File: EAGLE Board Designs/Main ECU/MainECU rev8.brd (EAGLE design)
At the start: 120.6 x 78.9 mm, 218 parts, among them J1 JUMPER, J2 JUMPER, J3 JUMPER, J4 JUMPER, J5 JUMPER, J6 JUMPER, J7 JUMPER, J8 JUMPER, P1 SOLDER_PAD, P2 SOLDER_PAD, Q1 P-CHANNEL_MOSFET_DMP3099L-7, Q12 P-CHANNEL_MOSFET_DMP3099L-7, X1 CONNECTOR-37, X2 CONNECTOR-4AUTOSPORT, X3 CONNECTOR-4NANO-FIT-VERTICAL-4, X4 CONNECTOR-4NANO-FIT-VERTICAL-4

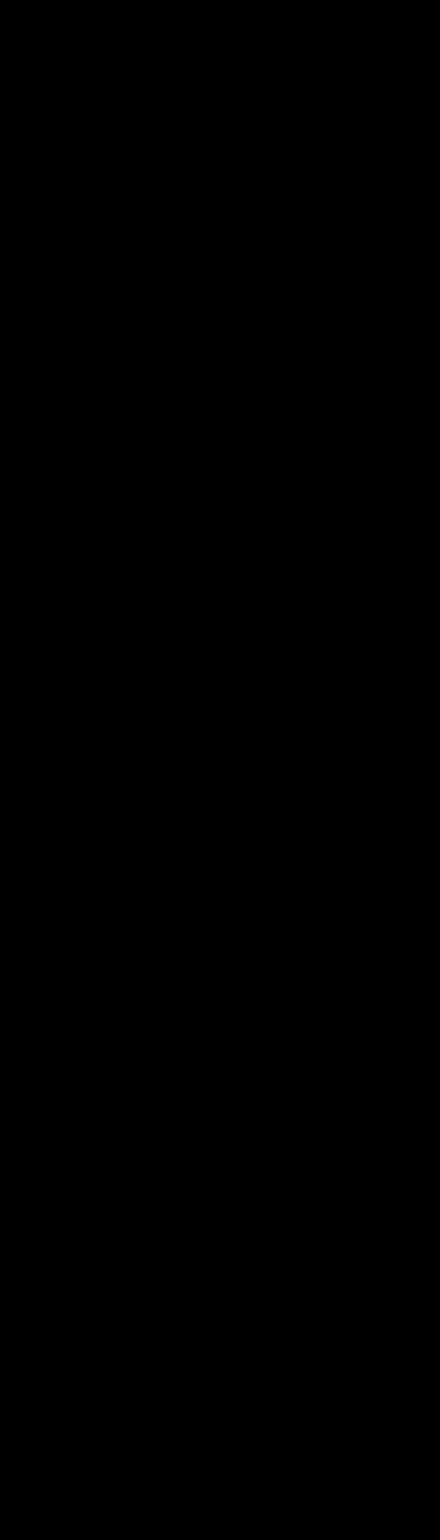
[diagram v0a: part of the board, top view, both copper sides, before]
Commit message: added BSPD schematic
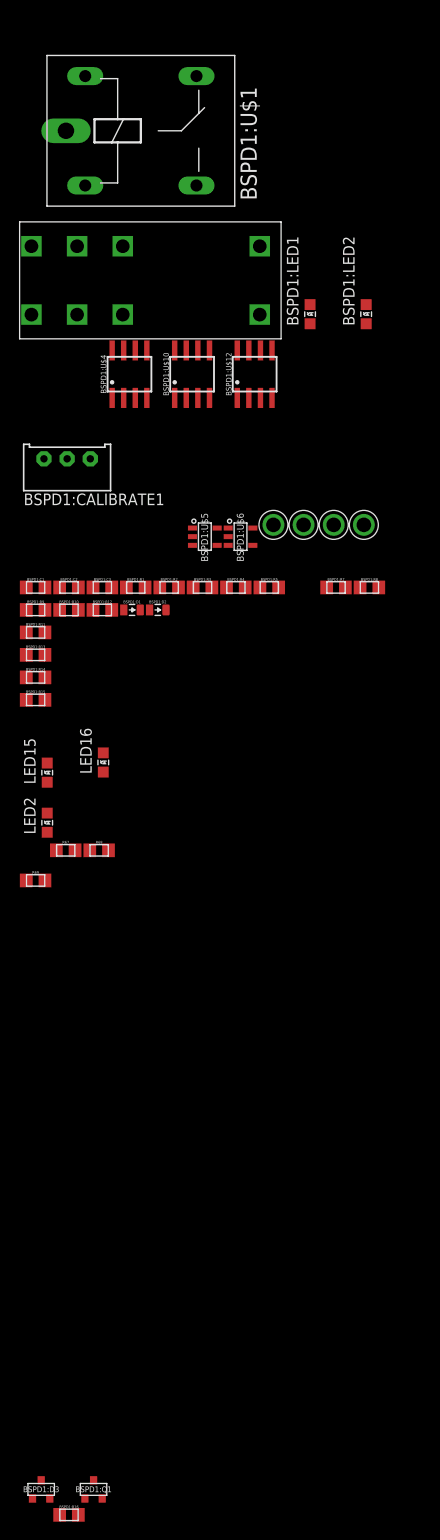
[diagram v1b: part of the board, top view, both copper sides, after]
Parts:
- added BSPD1:C1: .47µ, HyTechDevices:0805
- added BSPD1:C2, BSPD1:C3: 2.2µ, HyTechDevices:0805
- added BSPD1:CALIBRATE1: (no value), HyTechDevices:TRIMPOT_3296
- added BSPD1:D1, BSPD1:D2: DIODE0805, HyTechDevices:0805_D
- added BSPD1:D3: MMBZ5246BLT1G, HyTechDevices:SOT23
- added BSPD1:LED1, LED2: RED, HyTechDevices:LED-805
- added BSPD1:LED2, LED15: YELLOW, HyTechDevices:LED-805
- added BSPD1:Q1: (no value), HyTechDevices:SOT23
- added BSPD1:R1: 12k, HyTechDevices:0805
- added BSPD1:R10, BSPD1:R12: 100, HyTechDevices:0805
- added BSPD1:R11, BSPD1:R13, BSPD1:R14, BSPD1:R15: TBD, HyTechDevices:0805
- added BSPD1:R16, BSPD1:R4, BSPD1:R7: 10k, HyTechDevices:0805
- added BSPD1:R2: 43k, HyTechDevices:0805
- added BSPD1:R3: 330, HyTechDevices:0805
- added BSPD1:R5: 680k, HyTechDevices:0805
- added BSPD1:R8, BSPD1:R9, R67, R68: 270, HyTechDevices:0805
- added BSPD1:U$1: G5LE, HyTechDevices:ZF112
- added BSPD1:U$10, BSPD1:U$4: MCP6542SOIC, HyTechDevices:SOIC-08
- added BSPD1:U$11, BSPD1:U$13, U$14, U$15: TEST_POINT, HyTechDevices:TEST_POINT
- added BSPD1:U$12: MCP6002SOIC, HyTechDevices:SOIC-08
- added BSPD1:U$3: JW2SN-DC12V, HyTechDevices:JW2SN
- added BSPD1:U$5: SN74AHC1G09, HyTechDevices:SOT-23-5
- added BSPD1:U$6: SN74LVC1G08, HyTechDevices:SOT-23-5
- added LED16: GREEN, HyTechDevices:LED-805
- added R69: 200, HyTechDevices:0805
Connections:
- new net BSPD1:N$1: BSPD1:D1.A, BSPD1:Q1.3, BSPD1:U$3.COIL+
- new net BSPD1:N$10: BSPD1:D1.C
- new net BSPD1:N$13: BSPD1:C1.1, BSPD1:R3.1, BSPD1:R5.1, BSPD1:U$12.3, BSPD1:U$4.3
- new net BSPD1:N$14: BSPD1:LED2.C, BSPD1:R8.1
- new net BSPD1:N$15: BSPD1:LED1.C, BSPD1:R9.1
- new net BSPD1:N$16: BSPD1:LED1.A, BSPD1:U$10.7, BSPD1:U$11.P$1, BSPD1:U$5.2, BSPD1:U$6.2
- new net BSPD1:N$17: BSPD1:LED2.A, BSPD1:U$10.1, BSPD1:U$13.P$1, BSPD1:U$5.1, BSPD1:U$6.1
- new net BSPD1:N$2: BSPD1:R3.2, BSPD1:U$5.4
- new net BSPD1:N$3: BSPD1:D3.3, BSPD1:Q1.1, BSPD1:R16.1, BSPD1:U$4.1
- new net BSPD1:N$5: BSPD1:R14.2, BSPD1:R15.1, BSPD1:U$10.2
- new net BSPD1:N$6: BSPD1:CALIBRATE1.2, BSPD1:U$10.6
- new net BSPD1:N$7: BSPD1:R11.2, BSPD1:R13.1, BSPD1:U$4.2
- new net BSPD1:N$9: BSPD1:R1.2, BSPD1:R2.1, BSPD1:U$12.5
- new net BSPD1:SHUTDOWN_C: BSPD1:U$1.S, BSPD1:U$3.6
- new net BSPD1:SIGNAL_BRAKE_FILT: BSPD1:C3.2, BSPD1:R12.2, BSPD1:R4.2, BSPD1:U$10.5
- new net BSPD1:SIGNAL_CURRENT_FILT: BSPD1:C2.2, BSPD1:R10.2, BSPD1:R7.1, BSPD1:U$10.3
- new net N$64: LED2.C, R67.2
- new net N$76: LED15.C, R68.2
- new net N$77: LED16.C, R69.2
- new net READ_CHARGE: BSPD1:U$12.1, BSPD1:U$12.2, LED15.A
- new net READ_FAULT: BSPD1:U$12.6, BSPD1:U$12.7, LED16.A
- new net READ_SWITCH: BSPD1:U$6.4, LED2.A
- new net SIGNAL_CURRENT: BSPD1:R10.1, U$15.P$1
- net +12V: now also BSPD1:D2.C, BSPD1:R2.2, BSPD1:U$1.2, BSPD1:U$3.3, BSPD1:U$3.4, BSPD1:U$3.COIL-
- net +5V: now also BSPD1:CALIBRATE1.1, BSPD1:R13.2, BSPD1:R15.2, BSPD1:R4.1, BSPD1:R5.2, BSPD1:R7.2, BSPD1:U$10.8, BSPD1:U$12.8, BSPD1:U$4.8, BSPD1:U$5.5, BSPD1:U$6.5
- net GND: now also BSPD1:C1.2, BSPD1:C2.1, BSPD1:C3.1, BSPD1:CALIBRATE1.3, BSPD1:D2.A, BSPD1:D3.1, BSPD1:Q1.2, BSPD1:R1.1, BSPD1:R11.1, BSPD1:R14.1, BSPD1:R16.2, BSPD1:R8.2, BSPD1:R9.2, BSPD1:U$1.1, BSPD1:U$10.4, BSPD1:U$12.4, BSPD1:U$4.4, BSPD1:U$5.3, BSPD1:U$6.3, R67.1, R68.1, R69.1
- net SHUTDOWN_B: now also BSPD1:U$1.P
- net SHUTDOWN_D: now also BSPD1:U$3.7
- net SIGNAL_BRAKE: now also BSPD1:R12.1, U$14.P$1
